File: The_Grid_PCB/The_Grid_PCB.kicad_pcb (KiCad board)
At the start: 2 copper layers, 115 x 60 mm, 96 parts, among them J1 Screw_Terminal_01x02, J10 Screw_Terminal_01x02, J11 Screw_Terminal_01x02, J12 Screw_Terminal_01x02, J13 Screw_Terminal_01x02, J14 Screw_Terminal_01x02, J15 Screw_Terminal_01x02, J16 Screw_Terminal_01x02, J2 Screw_Terminal_01x03, J3 Screw_Terminal_01x03, J4 Screw_Terminal_01x02, J5 Screw_Terminal_01x02, J6 Screw_Terminal_01x02, J7 Screw_Terminal_01x02, J8 Screw_Terminal_01x02, J9 Screw_Terminal_01x02, Q1 AO3400A, Q10 AO3400A, Q11 AO3400A, Q12 AO3400A, Q2 AO3400A, Q3 AO3400A, Q4 AO3400A, Q5 AO3400A, Q6 AO3400A, Q7 AO3400A, Q8 AO3400A, Q9 AO3400A, U1 STM32 Blue Pill, U2 SN65HVD485EDR, U3 TPS54331DR

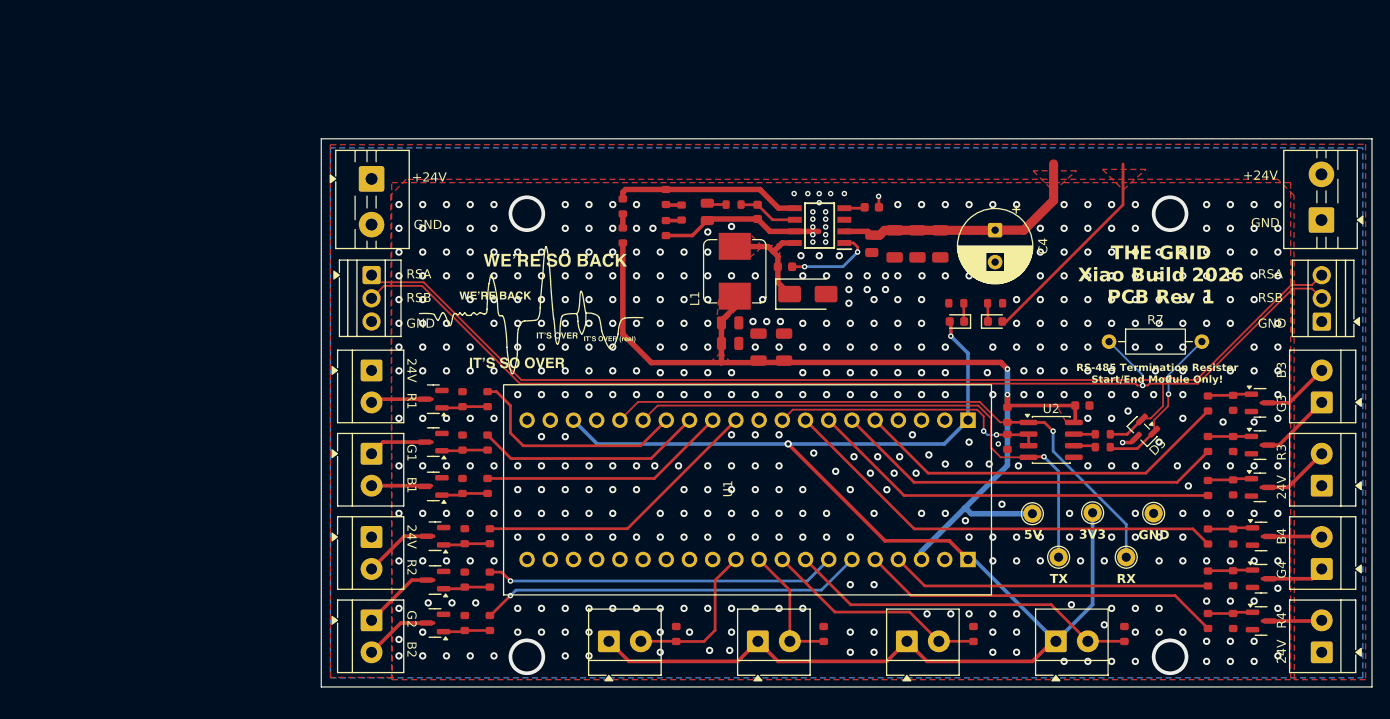
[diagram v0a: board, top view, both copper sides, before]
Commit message: pcb impedence matching, switch cap filtering, mounting holes, silkscreen updates
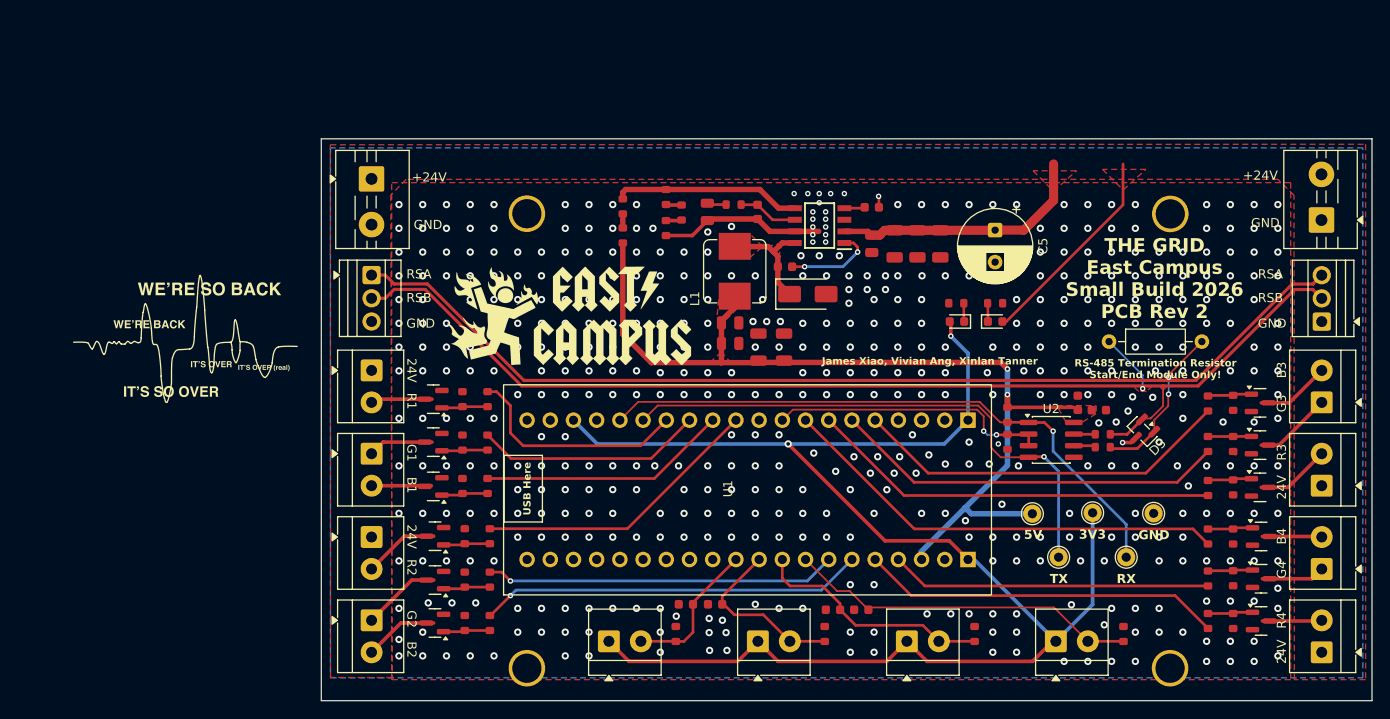
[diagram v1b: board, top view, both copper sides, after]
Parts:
- added C10: 100nF, PCM_JLCPCB:C_0603, F.Cu at (122.4, 121.0)
- added C11: 100nF, PCM_JLCPCB:C_0603, F.Cu at (125.6, 121.0)
- added C16: 100nF, PCM_JLCPCB:C_0603, F.Cu at (138.5, 121.5)
- added C17: 100nF, PCM_JLCPCB:C_0603, F.Cu at (141.6, 121.5)
- added C3: 100nF, PCM_JLCPCB:C_0603, F.Cu at (165.3, 98.9)
- added REF**: MountingHole_3.2mm_M3_DIN965_Pad, MountingHole:MountingHole_3.2mm_M3_DIN965_Pad, F.Cu at (105.0, 78.2)
- added REF**: MountingHole_3.2mm_M3_DIN965_Pad, MountingHole:MountingHole_3.2mm_M3_DIN965_Pad, F.Cu at (175.4, 128.0)
- added REF**: MountingHole_3.2mm_M3_DIN965_Pad, MountingHole:MountingHole_3.2mm_M3_DIN965_Pad, F.Cu at (105.0, 128.0)
- added REF**: MountingHole_3.2mm_M3_DIN965_Pad, MountingHole:MountingHole_3.2mm_M3_DIN965_Pad, F.Cu at (175.4, 78.2)
- moved C2 1.87 mm to (167.6, 99.7)
- moved R16 0.12 mm to (154.0, 124.2)
- moved R9 0.11 mm to (137.6, 124.2)
- moved R17 0.10 mm to (170.3, 124.2)
- renumbered C9 to C12, C10 to C13, C11 to C14, C12 to C15, C13 to C18, C14 to C19, C3 to C4, C4 to C5, C5 to C6, C6 to C7, C7 to C8, C8 to C9
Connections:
- net /RSA renamed /RS+
- net /RSB renamed /RS-
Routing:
- net /Microswitch2: track 14.1 -> 19.4 mm
- net +5V: track 104.0 -> 101.8 mm
- net /Microswitch3: track 24.6 -> 26.2 mm
- net /Microswitch1: track 17.3 -> 16.0 mm
- net GND: vias 506 -> 501
- added copper zone on F.Cu, net /RS+
- added copper zone on F.Cu, net /RS-
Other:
- board size 115 x 60 mm -> 115 x 61.5 mm
- board text added: "James Xiao, Vivian Ang, Xinlan Tanner"
- board text added: "THE GRID East Campus Small Build 2026 PCB Rev 2"
- board text added: "USB Here"
- board text removed: "THE GRID Xiao Build 2026 PCB Rev 1"

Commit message: rev2 minus silkscreen
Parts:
- removed the D2 at (156.2, 90.0)
- removed the R2 at (156.2, 88.0)
- R1: value 220Ω -> 560Ω
- moved R1 0.09 mm to (152.1, 88.0)
- renumbered D3 to D2, D4 to D3, R11 to R10, R12 to R11, R13 to R12, R14 to R13, R15 to R14, R16 to R15, R17 to R16, R18 to R17, R19 to R18, R20 to R19, R3 to R2, R21 to R20, R22 to R21, R23 to R22, R24 to R23, R25 to R24, R26 to R25, R27 to R26, R28 to R27, R29 to R28, R30 to R29, R4 to R3, R31 to R30, R32 to R31, R33 to R32, R34 to R33, R35 to R34, R36 to R35, R37 to R36, R38 to R37, R39 to R38, R40 to R39, R5 to R4, R41 to R40, R6 to R5, R7 to R6, R8 to R7, R9 to R8, R10 to R9
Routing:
- net +24V: track 52.3 -> 29.4 mm
- net Net-(D2-K): track 1.97 -> 0.00 mm
- net GND: track 23.5 -> 25.0 mm, vias 501 -> 504
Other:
- board text added: "3V3 Power"
- board text added: "BUILD IS SO BACK!!!!"
- board text added: "IT'S SO OVER"
- board text added: "STM32 Blue Pill"
- board text added: "Switch 1"
- board text added: "Switch 2"
- board text added: "Switch 3"
- board text added: "Switch 4"
- board text added: "WE'RE SO BACK"
- board text added: "小"

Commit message: pcb rev 2 ready for fab (?)
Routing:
- net GND: vias 504 -> 503
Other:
- board text removed: "BUILD IS SO BACK!!!!"
- board text removed: "IT'S SO OVER"
- board text removed: "WE'RE SO BACK"
- board text removed: "小"

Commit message: pcb rev2 sent to fab
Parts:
- U2: value SN65HVD485EDR -> THDV1520
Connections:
- U1 pad 20: GND -> unconnected-(U1-GND-Pad20)
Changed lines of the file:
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@@
 			)
 		)
-		(property "Value" "SN65HVD485EDR"
+		(property "Value" "THDV1520"
 			(at 0 3.4 0)
 			(layer "F.Fab")
@@
 			)
 		)
-		(property "Datasheet" "http://www.ti.com/lit/gpn/sn65hvd485e"
+		(property "Datasheet" "https://www.ti.com/lit/ds/symlink/thvd1520.pdf?ts=1784928696084&ref_url=https%253A%252F%252Fwww.ti.com"
 			(at 0 0 0)
 			(layer "F.Fab")
@@
 			)
 		)
-		(property "Manufacturer_Part_Number" "SN65HVD485EDR"
+		(property "Manufacturer_Part_Number" "THDV1520"
 			(at 0 0 0)
 			(unlocked yes)
@@
 			)
 		)
-		(property "LCSC" "C27899"
+		(property "LCSC" "C882408"
 			(at 0 0 0)
 			(unlocked yes)
@@
 			(layers "*.Cu" "*.Mask")
 			(remove_unused_layers no)
-			(net "GND")
+			(net "unconnected-(U1-GND-Pad20)")
 			(pinfunction "GND_20")
-			(pintype "passive")
+			(pintype "passive+no_connect")
 		)
 		(pad "21" thru_hole circle
@@
 	)
 	(segment
+		(start 132.95 118.1)
+		(end 132.96 118.09)
+		(width 0.3)
+		(layer "F.Cu")
+		(net "/Microswitch3")
+	)
+	(segment
 		(start 153.858456 125)
 		(end 153.878456 125.02)
@@
 	(segment
 		(start 139.28 120.88)
-		(end 137.35 118.95)
+		(end 138.85 120.45)
 		(width 0.3)
 		(layer "F.Cu")
@@
 	)
 	(segment
-		(start 132.96 118.09)
-		(end 132.96 116.05)
+		(start 135.3 120.45)
+		(end 132.95 118.1)
 		(width 0.3)
 		(layer "F.Cu")
@@
 	)
 	(segment
-		(start 139.28 121.55)
-		(end 139.28 120.88)
+		(start 138.85 120.45)
+		(end 135.3 120.45)
 		(width 0.3)
 		(layer "F.Cu")
@@
 	)
 	(segment
-		(start 132.95 118.1)
-		(end 132.96 118.09)
-		(width 0.3)
-		(layer "F.Cu")
-		(net "/Microswitch3")
-	)
-	(segment
-		(start 137.35 118.95)
-		(end 133.8 118.95)
+		(start 139.28 121.55)
+		(end 139.28 120.88)
 		(width 0.3)
 		(layer "F.Cu")
@@
 	)
 	(segment
-		(start 133.8 118.95)
-		(end 132.95 118.1)
+		(start 132.96 118.09)
+		(end 132.96 116.05)
 		(width 0.3)
 		(layer "F.Cu")
@@
 	)
 	(segment
+		(start 135.5 116.05)
+		(end 138.55 119.1)
+		(width 0.3)
+		(layer "F.Cu")
+		(net "/Microswitch4")
+	)
+	(segment
 		(start 166.4 125)
 		(end 170.38 125)
@@
 	)
 	(segment
-		(start 135.5 116.05)
-		(end 138.95 119.5)
+		(start 139.93 119.1)
+		(end 142.38 121.55)
 		(width 0.3)
 		(layer "F.Cu")
@@
 	)
 	(segment
-		(start 138.95 119.5)
-		(end 140.33 119.5)
-		(width 0.3)
-		(layer "F.Cu")
-		(net "/Microswitch4")
-	)
-	(segment
-		(start 140.33 119.5)
-		(end 142.38 121.55)
+		(start 138.55 119.1)
+		(end 139.93 119.1)
 		(width 0.3)
 		(layer "F.Cu")
